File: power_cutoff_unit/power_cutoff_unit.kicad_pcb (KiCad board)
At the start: 2 copper layers, 0 parts

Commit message: 何したか覚えてないけど。
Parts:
- added BZ1: Buzzer, Buzzer_Beeper:Buzzer_12x9.5RM7.6, F.Cu at (213.0, 103.5)
- added C1: 0.022uF, Capacitor_SMD:C_0402_1005Metric, F.Cu at (103.9, 137.6)
- added C10: 1000u, Capacitor_THT:CP_Radial_D16.0mm_P7.50mm, F.Cu at (269.7, 84.0)
- added C11: 0.1u, Capacitor_SMD:C_0402_1005Metric, F.Cu at (103.9, 143.5)
- added C12: 10uF, Capacitor_SMD:C_0805_2012Metric, F.Cu at (177.0, 86.1)
- added C16: 0.1u, Capacitor_SMD:C_0402_1005Metric, F.Cu at (106.7, 137.6)
- added C18: 4.7uF, Capacitor_SMD:C_0603_1608Metric, F.Cu at (116.3, 123.3)
- added C2: 4700pF, Capacitor_SMD:C_0402_1005Metric, F.Cu at (103.9, 139.6)
- added C20: 0.1u, Capacitor_SMD:C_0402_1005Metric, F.Cu at (106.7, 139.6)
- added C21: 0.1u, Capacitor_SMD:C_0402_1005Metric, F.Cu at (106.7, 141.5)
- added C22: 4.7u, Capacitor_SMD:C_0805_2012Metric, F.Cu at (177.0, 89.1)
- added C23: 1u, Capacitor_SMD:C_0402_1005Metric, F.Cu at (106.7, 143.5)
- added C24: 0.1u, Capacitor_SMD:C_0402_1005Metric, F.Cu at (109.6, 137.6)
- added C25: 4.7u, Capacitor_SMD:C_0805_2012Metric, F.Cu at (177.0, 92.1)
- added C26: 4.7u, Capacitor_SMD:C_0805_2012Metric, F.Cu at (177.0, 95.2)
- added C27: 0.1u, Capacitor_SMD:C_0402_1005Metric, F.Cu at (109.6, 139.6)
- added C28: 0.1u, Capacitor_SMD:C_0402_1005Metric, F.Cu at (109.6, 141.5)
- added C29: 0.1u, Capacitor_SMD:C_0402_1005Metric, F.Cu at (109.6, 143.5)
- added C3: 1uF, Capacitor_SMD:C_0402_1005Metric, F.Cu at (103.9, 141.5)
- added C30: 0.1u, Capacitor_SMD:C_0402_1005Metric, F.Cu at (112.5, 137.6)
- added C31: 0.1u, Capacitor_SMD:C_0402_1005Metric, F.Cu at (112.5, 139.6)
- added C32: 0.1u, Capacitor_SMD:C_0402_1005Metric, F.Cu at (112.5, 141.5)
- added C33: 4.7u, Capacitor_SMD:C_0603_1608Metric, F.Cu at (116.3, 125.9)
- added C34: 1u, Capacitor_SMD:C_0402_1005Metric, F.Cu at (112.5, 143.5)
- added C4: 47uF, Capacitor_SMD:C_1210_3225Metric, F.Cu at (224.5, 114.8)
- added C5: 47uF, Capacitor_SMD:C_1210_3225Metric, F.Cu at (224.5, 119.0)
- added C6: 10uF, Capacitor_SMD:C_0805_2012Metric, F.Cu at (177.0, 80.1)
- added C7: 470u, Capacitor_THT:CP_Radial_D12.5mm_P5.00mm, F.Cu at (244.2, 79.0)
- added C8: 10uF, Capacitor_SMD:C_0805_2012Metric, F.Cu at (177.0, 83.1)
- added D10: LED, LED_SMD:LED_0603_1608Metric, F.Cu at (139.2, 87.5)
- added D14: LED, LED_SMD:LED_0603_1608Metric, F.Cu at (139.2, 90.1)
- added D15: Blue, LED_SMD:LED_0603_1608Metric_Pad1.05x0.95mm_HandSolder, F.Cu at (197.1, 108.0)
- added D16: LED, LED_SMD:LED_0603_1608Metric, F.Cu at (139.2, 92.7)
- added D17: SS2040FL, Diode_SMD:D_SOD-123F, F.Cu at (172.6, 106.4)
- added D18: LED, LED_SMD:LED_0603_1608Metric, F.Cu at (139.2, 95.3)
- added D19: LED, LED_SMD:LED_0603_1608Metric, F.Cu at (192.8, 82.5)
- added D2: LED, LED_SMD:LED_0603_1608Metric, F.Cu at (135.2, 87.5)
- added D20: LED, LED_SMD:LED_0603_1608Metric, F.Cu at (192.8, 60.8)
- added D21: LED, LED_SMD:LED_0603_1608Metric, F.Cu at (192.8, 65.0)
- added D22: LED, LED_SMD:LED_0603_1608Metric, F.Cu at (192.8, 69.0)
- added D23: LED, LED_SMD:LED_0603_1608Metric, F.Cu at (192.8, 73.0)
- added D24: LED, LED_SMD:LED_0603_1608Metric, F.Cu at (192.8, 77.5)
- added D3: LED, LED_SMD:LED_0603_1608Metric, F.Cu at (135.2, 90.1)
- added D4: LED, LED_SMD:LED_0603_1608Metric, F.Cu at (135.2, 92.7)
- added D5: SS2040FL, Diode_SMD:D_SOD-123F, F.Cu at (172.6, 99.7)
- added D6: LED, LED_SMD:LED_0603_1608Metric, F.Cu at (135.2, 95.3)
- added D7: LED, LED_SMD:LED_0603_1608Metric, F.Cu at (135.2, 97.9)
- added D8: SS2040FL, Diode_SMD:D_SOD-123F, F.Cu at (172.6, 103.1)
- added D9: LED, LED_SMD:LED_0603_1608Metric, F.Cu at (139.2, 84.9)
- added J1: Conn_01x02, Connector_AMASS:AMASS_XT60IPW-M_1x03_P7.20mm_Horizontal, F.Cu at (284.1, 126.8)
- added J10: Conn_01x02, Connector_AMASS:AMASS_XT30PW-M_1x02_P2.50mm_Horizontal, F.Cu at (219.0, 129.5)
- added J11: Conn_01x02_Pin, Connector_PinHeader_2.54mm:PinHeader_1x02_P2.54mm_Vertical, F.Cu at (203.5, 76.5)
- added J12: Conn_01x04, Connector_JST:JST_XH_B4B-XH-A_1x04_P2.50mm_Vertical, F.Cu at (197.5, 68.5)
- added J13: Conn_01x04, Connector_JST:JST_XH_B4B-XH-A_1x04_P2.50mm_Vertical, F.Cu at (197.5, 82.0)
- added J14: Conn_01x04, Connector_JST:JST_XH_B4B-XH-A_1x04_P2.50mm_Vertical, F.Cu at (224.5, 72.5)
- added J15: Conn_01x02, Connector_JST:JST_XH_B2B-XH-A_1x02_P2.50mm_Vertical, F.Cu at (204.5, 52.0)
- added J16: Conn_01x02, Connector_JST:JST_XH_B2B-XH-A_1x02_P2.50mm_Vertical, F.Cu at (213.2, 52.0)
- added J18: Conn_01x02, Connector_JST:JST_XH_B2B-XH-A_1x02_P2.50mm_Vertical, F.Cu at (222.0, 52.0)
- added J19: Conn_01x03, Connector_JST:JST_XH_B3B-XH-A_1x03_P2.50mm_Vertical, F.Cu at (207.0, 140.0)
- added J2: Conn_01x02, Connector_AMASS:AMASS_XT60IPW-M_1x03_P7.20mm_Horizontal, F.Cu at (246.6, 126.8)
- added J20: Conn_01x03, Connector_JST:JST_XH_B3B-XH-A_1x03_P2.50mm_Vertical, F.Cu at (197.5, 93.0)
- added J4: Conn_01x02, Connector_AMASS:AMASS_XT60PW-F_1x02_P7.20mm_Horizontal, F.Cu at (276.8, 65.7)
- added J6: Conn_01x02, Connector_AMASS:AMASS_XT60PW-F_1x02_P7.20mm_Horizontal, F.Cu at (251.1, 65.2)
- added JP1: SolderJumper_2_Open, Jumper:SolderJumper-2_P1.3mm_Open_RoundedPad1.0x1.5mm, B.Cu at (215.3, 72.5)
- added JP2: SolderJumper_2_Open, Jumper:SolderJumper-2_P1.3mm_Open_RoundedPad1.0x1.5mm, B.Cu at (215.3, 76.0)
- added JP3: SolderJumper_2_Open, Jumper:SolderJumper-2_P1.3mm_Open_RoundedPad1.0x1.5mm, B.Cu at (215.3, 79.6)
- added K1: T9GS1L14-5, GN10RELAY:T9G, F.Cu at (283.2, 113.2)
- added K2: G5Q-1-DC5, GN10RELAY:G5Q-1, F.Cu at (254.9, 109.8)
- added L1: 4.7u, GN10:DEM2818C, F.Cu at (217.0, 116.0)
- added Q1: SSM3K341R, Package_TO_SOT_SMD:SOT-23_Handsoldering, B.Cu at (227.5, 97.3)
- added Q2: SSM3K341R, Package_TO_SOT_SMD:SOT-23_Handsoldering, B.Cu at (227.5, 102.0)
- added Q3: SSM3K341R, Package_TO_SOT_SMD:SOT-23_Handsoldering, B.Cu at (227.5, 106.8)
- added Q5: BSS138, Package_TO_SOT_SMD:SOT-23, F.Cu at (207.6, 91.5)
- added R1: 100K, Resistor_SMD:R_0603_1608Metric, F.Cu at (116.3, 128.4)
- added R10: 1K, Resistor_SMD:R_0603_1608Metric, F.Cu at (120.3, 123.3)
- added R11: 20K, Resistor_SMD:R_0603_1608Metric, F.Cu at (120.3, 125.9)
- added R12: 4.7K, Resistor_SMD:R_0603_1608Metric, F.Cu at (120.3, 128.4)
- added R13: 470, Resistor_SMD:R_0603_1608Metric, F.Cu at (120.3, 130.9)
- added R14: 20K, Resistor_SMD:R_0603_1608Metric, F.Cu at (120.3, 133.4)
- added R15: 25, Package_TO_SOT_THT:TO-220-2_Vertical, F.Cu at (258.2, 91.0)
- added R16: 1K, Resistor_SMD:R_0402_1005Metric, F.Cu at (171.5, 64.0)
- added R17: 1K, Resistor_SMD:R_0603_1608Metric, F.Cu at (120.3, 135.9)
- added R18: 20K, Resistor_SMD:R_0603_1608Metric, F.Cu at (120.3, 138.4)
- added R19: 1K, Resistor_SMD:R_0402_1005Metric, F.Cu at (171.5, 66.0)
- added R2: 34K, Resistor_SMD:R_0402_1005Metric, F.Cu at (171.5, 58.0)
- added R20: 25, Package_TO_SOT_THT:TO-220-2_Vertical, F.Cu at (242.0, 96.4)
- added R21: 4.7K, Resistor_SMD:R_0603_1608Metric, F.Cu at (120.3, 140.9)
- added R27: 20K, Resistor_SMD:R_0603_1608Metric, F.Cu at (124.3, 123.3)
- added R28: 20K, Resistor_SMD:R_0603_1608Metric, F.Cu at (124.3, 125.9)
- added R29: 20K, Resistor_SMD:R_0603_1608Metric, F.Cu at (124.3, 128.4)
- added R3: 24K, Resistor_SMD:R_0603_1608Metric, F.Cu at (116.3, 130.9)
- added R30: 20K, Resistor_SMD:R_0603_1608Metric, F.Cu at (124.3, 130.9)
- added R31: 1K, Resistor_SMD:R_0603_1608Metric, F.Cu at (124.3, 133.4)
- added R32: 1K, Resistor_SMD:R_0603_1608Metric, F.Cu at (124.3, 135.9)
- added R33: 1K, Resistor_SMD:R_0603_1608Metric, F.Cu at (124.3, 138.4)
- added R34: 120, Resistor_SMD:R_0603_1608Metric, F.Cu at (124.3, 140.9)
- added R35: 1K, Resistor_SMD:R_0603_1608Metric, F.Cu at (128.3, 123.3)
- added R36: 10K, Resistor_SMD:R_0603_1608Metric, F.Cu at (128.3, 125.9)
- added R37: 470, Resistor_SMD:R_0603_1608Metric, F.Cu at (128.3, 128.4)
- added R38: 20K, Resistor_SMD:R_0603_1608Metric, F.Cu at (128.3, 130.9)
- added R39: 1K, Resistor_SMD:R_0603_1608Metric, F.Cu at (128.3, 133.4)
- added R4: 4.7K, Resistor_SMD:R_0603_1608Metric, F.Cu at (116.3, 133.4)
- added R40: 1K, Resistor_SMD:R_0603_1608Metric, F.Cu at (128.3, 135.9)
- added R41: 1K, Resistor_SMD:R_0603_1608Metric, F.Cu at (128.3, 138.4)
- added R42: 1K, Resistor_SMD:R_0603_1608Metric, F.Cu at (128.3, 140.9)
- added R43: 1K, Resistor_SMD:R_0603_1608Metric, F.Cu at (132.3, 123.3)
- added R44: 1K, Resistor_SMD:R_0603_1608Metric, F.Cu at (132.3, 125.9)
- added R45: 10K, Resistor_SMD:R_0603_1608Metric, F.Cu at (132.3, 128.4)
- added R46: 10K, Resistor_SMD:R_0603_1608Metric, F.Cu at (132.3, 130.9)
- added R47: 10K, Resistor_SMD:R_0603_1608Metric, F.Cu at (132.3, 133.4)
- added R48: 10K, Resistor_SMD:R_0603_1608Metric, F.Cu at (132.3, 135.9)
- added R49: 10K, Resistor_SMD:R_0603_1608Metric, F.Cu at (132.3, 138.4)
- added R5: 6.49K, Resistor_SMD:R_0402_1005Metric, F.Cu at (171.5, 60.0)
- added R7: 4.7K, Resistor_SMD:R_0603_1608Metric, F.Cu at (116.3, 138.4)
- added R8: 4.7K, Resistor_SMD:R_0603_1608Metric, F.Cu at (116.3, 140.9)
- added R9: 1K, Resistor_SMD:R_0402_1005Metric, F.Cu at (171.5, 62.0)
- added SW1: SW_Push, GN10:SKRPABE010, F.Cu at (200.1, 54.0)
- added SW2: SW_DIP_x02, Button_Switch_SMD:SW_DIP_SPSTx02_Slide_Omron_A6H-2101_W6.15mm_P1.27mm, F.Cu at (216.4, 62.1)
- added SW3: SW_DIP_x02, Button_Switch_SMD:SW_DIP_SPSTx02_Slide_Omron_A6H-2101_W6.15mm_P1.27mm, F.Cu at (195.0, 139.0)
- added U1: LMZ14201H, GN10:LMZ14201H, F.Cu at (258.0, 136.5)
- added U3: MIC4427, Package_SO:SOIC-8_3.9x4.9mm_P1.27mm, B.Cu at (228.0, 90.9)
- added U4: ADuM120N, Package_SO:SOIC-8_3.9x4.9mm_P1.27mm, F.Cu at (223.0, 83.1)
- added U5: LMR50410Y3FQDBVRQ1, Package_TO_SOT_SMD:SOT-23-6, F.Cu at (217.5, 121.1)
- added U6: MCP2562-E-SN, Package_SO:SOIC-8_3.9x4.9mm_P1.27mm, F.Cu at (207.0, 63.5)
- added U7: STM32F303K8Tx, Package_QFP:LQFP-32_7x7mm_P0.8mm, F.Cu at (215.0, 73.0)
- added U8: MOUDLE-SEEEDUINO-XIAO-ESP32C3, RF_Module:MCU_Seeed_ESP32C3, F.Cu at (202.9, 121.0)

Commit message: PCBに入ったけどコンデンサの放電用抵抗を小さくしたい。
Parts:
- removed U8: MOUDLE-SEEEDUINO-XIAO-ESP32C3, RF_Module:MCU_Seeed_ESP32C3
- added U2: MOUDLE-SEEEDUINO-XIAO-ESP32C3, RF_Module:MCU_Seeed_ESP32C3, F.Cu at (-132.0, 145.6)
- C1: value 0.022uF -> 0.022u
- C12: value 10uF -> 10u
- C18: value 4.7uF -> 4.7u
- C2: value 4700pF -> 4700p
- J1, J2: footprint Connector_AMASS:AMASS_XT60IPW-M_1x03_P7.20mm_Horizontal -> Connector_AMASS:AMASS_XT60PW-M_1x02_P7.20mm_Horizontal
- JP1, JP2, JP3, Q1, Q2, Q3, U3: moved to F.Cu
- R15, R20: value 25 -> 30; footprint Package_TO_SOT_THT:TO-220-2_Vertical -> Package_TO_SOT_SMD:TO-263-2_TabPin1
- moved J1 547.4 mm to (-256.8, 42.3), turned to 0 degrees
- moved J2 493.1 mm to (-239.2, 42.3), turned to 0 degrees
- moved U1 486.2 mm to (-226.0, 90.3), turned to 0 degrees
- moved C4 483.7 mm to (-258.2, 84.7)
- moved C5 483.7 mm to (-258.2, 89.0)
- moved L1 472.2 mm to (-252.6, 165.9)
- moved U6 470.6 mm to (-245.4, 193.0)
- moved U5 457.3 mm to (-237.8, 163.8), turned to 0 degrees
- moved K1 456.8 mm to (-169.2, 49.8), turned to 0 degrees
- moved J11 452.6 mm to (-234.2, 191.7)
- moved J10 445.3 mm to (-225.9, 147.2), turned to 0 degrees
- moved J12 430.6 mm to (-216.4, 187.4), turned to 0 degrees
- moved R2 429.5 mm to (-256.6, 92.7)
- moved R5 429.5 mm to (-256.6, 94.7)
- moved J13 429.1 mm to (-216.4, 195.2), turned to 0 degrees
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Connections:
- net VDD renamed +5VA

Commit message: 配置考え始めた
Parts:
- removed C11: 0.1u, Capacitor_SMD:C_0402_1005Metric
- removed C3: 1uF, Capacitor_SMD:C_0402_1005Metric
- removed J18: Conn_01x02, Connector_JST:JST_XH_B2B-XH-A_1x02_P2.50mm_Vertical
- removed J19: Conn_01x03, Connector_JST:JST_XH_B3B-XH-A_1x03_P2.50mm_Vertical
- removed R49: 10K, Resistor_SMD:R_0603_1608Metric
- D8, Q2, R13, R14, R20, R34, R47, R48, U6: moved to B.Cu
- J10: footprint Connector_AMASS:AMASS_XT30PW-M_1x02_P2.50mm_Horizontal -> Connector_AMASS:AMASS_XT30U-M_1x02_P5.0mm_Vertical
- R15: value 30 -> 50; moved to B.Cu
- R3, R32, R4: footprint Resistor_SMD:R_0603_1608Metric -> Resistor_SMD:R_0402_1005Metric
- moved R7 439.6 mm to (193.5, 62.5), turned to 180 degrees
- moved J2 427.4 mm to (187.9, 57.6)
- moved J1 423.5 mm to (166.4, 57.6)
- moved D2 416.9 mm to (190.5, 62.5)
- moved R8 405.6 mm to (159.5, 55.2), turned to -90 degrees
- moved C5 399.3 mm to (140.6, 70.0)
- moved C4 399.3 mm to (140.6, 66.5)
- moved R2 393.1 mm to (135.5, 65.5), turned to 180 degrees
- moved R5 391.2 mm to (133.5, 65.5)
- moved R1 390.2 mm to (135.5, 56.0), turned to -90 degrees
- moved R3 388.4 mm to (133.5, 56.0), turned to 180 degrees
- moved R4 386.7 mm to (131.5, 56.0), turned to 180 degrees
- moved D3 385.4 mm to (159.5, 58.3), turned to 90 degrees
- moved C6 383.5 mm to (140.6, 52.5)
- moved C1 379.3 mm to (135.5, 67.5), turned to 180 degrees
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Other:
- board outline added: 100 x 75 mm

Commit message: PCBの配置考え中
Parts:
- J14: footprint Connector_JST:JST_XH_B4B-XH-A_1x04_P2.50mm_Vertical -> Connector_PinHeader_2.54mm:PinHeader_1x04_P2.54mm_Vertical
- J20: footprint Connector_JST:JST_XH_B3B-XH-A_1x03_P2.50mm_Vertical -> Connector_PinHeader_2.54mm:PinHeader_1x03_P2.54mm_Vertical
- R15, R20: moved to F.Cu
- moved R11 91.5 mm to (67.2, 126.5)
- moved R27 91.5 mm to (59.7, 139.0)
- moved R28 91.5 mm to (59.7, 137.0)
- moved C12 91.5 mm to (104.0, 121.5)
- moved C16 91.5 mm to (71.0, 136.0)
- moved C18 91.5 mm to (71.0, 134.5)
- moved C20 91.5 mm to (60.0, 142.0)
- moved C21 91.5 mm to (65.0, 142.0)
- moved C22 91.5 mm to (7.00, 91.4)
- moved C23 91.5 mm to (-8.53, 98.4)
- moved C24 91.5 mm to (-5.66, 92.5)
- moved C25 91.5 mm to (7.00, 94.4)
- moved C26 91.5 mm to (7.00, 97.4)
- moved C27 91.5 mm to (-113.5, 181.7)
- moved C28 91.5 mm to (-113.5, 183.6)
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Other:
- board size 100 x 75 mm -> 237 x 99 mm

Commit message: 大電流部品の主な配置を考えた。
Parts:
- added REF**: MountingHole_3.2mm_M3, MountingHole:MountingHole_3.2mm_M3, F.Cu at (123.5, 67.5)
- added REF**: MountingHole_3.2mm_M3, MountingHole:MountingHole_3.2mm_M3, F.Cu at (215.5, 134.5)
- added REF**: MountingHole_3.2mm_M3, MountingHole:MountingHole_3.2mm_M3, F.Cu at (123.5, 134.5)
- added REF**: MountingHole_3.2mm_M3, MountingHole:MountingHole_3.2mm_M3, F.Cu at (215.5, 67.5)
- R15: moved to B.Cu
- moved J10 110.8 mm to (130.2, 67.3), turned to 0 degrees
- moved K2 58.9 mm to (197.5, 81.9), turned to 0 degrees
- moved U2 51.7 mm to (137.8, 178.7)
- moved R15 47.3 mm to (187.4, 94.6), turned to 0 degrees
- moved J16 44.0 mm to (118.9, 165.7)
- moved R20 43.1 mm to (201.3, 102.3), turned to -90 degrees
- moved J15 35.2 mm to (133.5, 158.7)
- moved J2 33.8 mm to (200.1, 75.7)
- moved J6 32.9 mm to (199.0, 129.9)
- moved C7 32.6 mm to (205.5, 120.0)
- moved K1 30.3 mm to (168.7, 88.4)
- moved BZ1 30.0 mm to (145.2, 119.0)
- moved J12 30.0 mm to (123.0, 121.0)
- moved J13 30.0 mm to (123.0, 107.0)
- moved J14 30.0 mm to (149.0, 100.9)
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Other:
- board size 237 x 99 mm -> 207 x 86 mm

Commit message: 重要な制御系部品の配置を少し考えた。
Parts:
- C16, C18, U3: moved to B.Cu
- moved L1 162.4 mm to (130.3, 80.5)
- moved U5 149.7 mm to (132.1, 76.7), turned to 180 degrees
- moved C23 139.5 mm to (129.3, 76.7), turned to -90 degrees
- moved C24 139.4 mm to (133.1, 79.0), turned to 180 degrees
- moved D17 132.5 mm to (132.1, 73.7)
- moved SW3 131.5 mm to (152.4, 120.7), turned to -90 degrees
- moved C26 131.3 mm to (137.1, 80.3), turned to 90 degrees
- moved C25 128.9 mm to (135.1, 80.3), turned to 90 degrees
- moved C22 121.6 mm to (127.7, 76.7), turned to -90 degrees
- moved U3 112.8 mm to (173.4, 96.6)
- moved C16 110.0 mm to (171.9, 92.1), turned to 180 degrees
- moved C18 110.0 mm to (171.9, 90.6), turned to 180 degrees
- moved C20 109.6 mm to (159.6, 96.2)
- moved C21 109.0 mm to (163.4, 95.0)
- moved R27 108.7 mm to (158.3, 93.2)
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
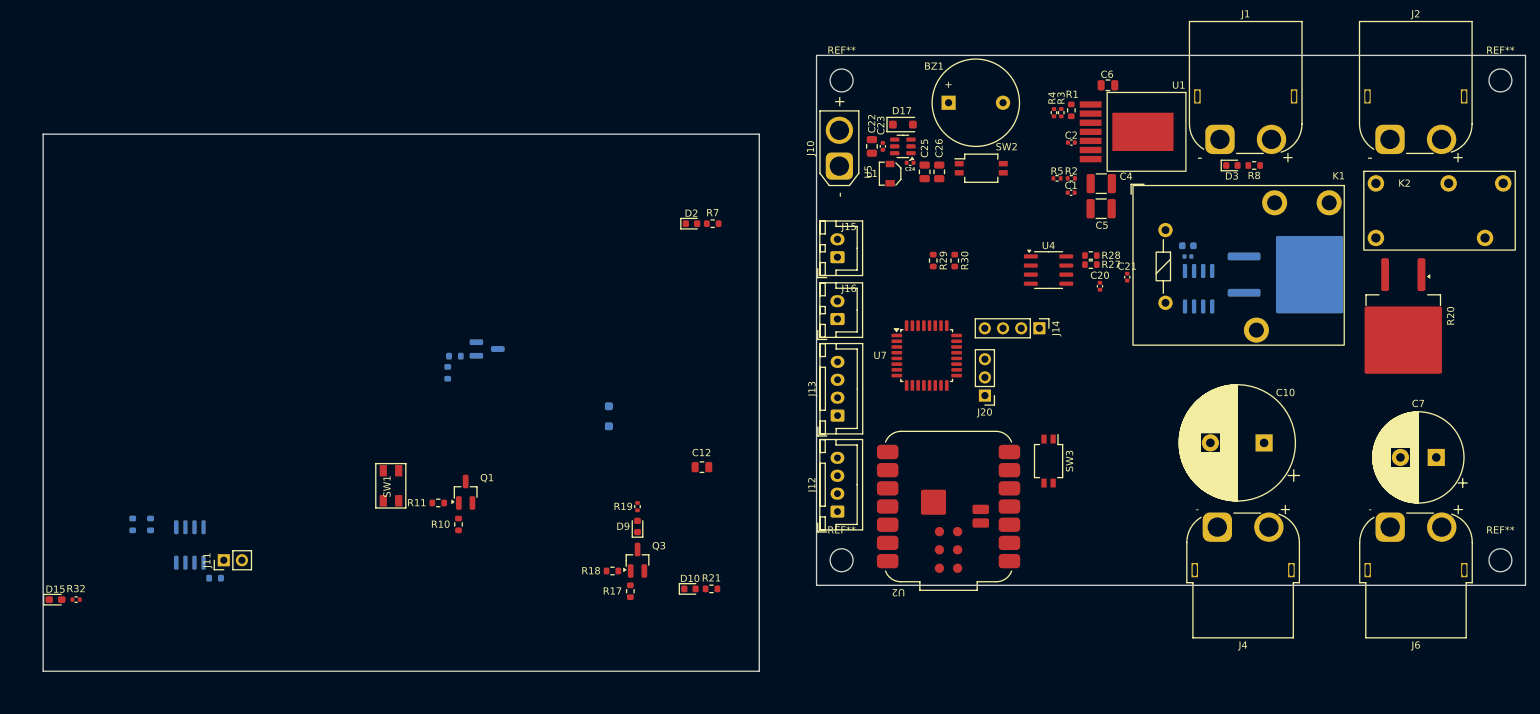
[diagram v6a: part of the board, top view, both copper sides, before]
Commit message: 高額だし、大きいので5Vラインのスイッチングレギュレーターを変更。
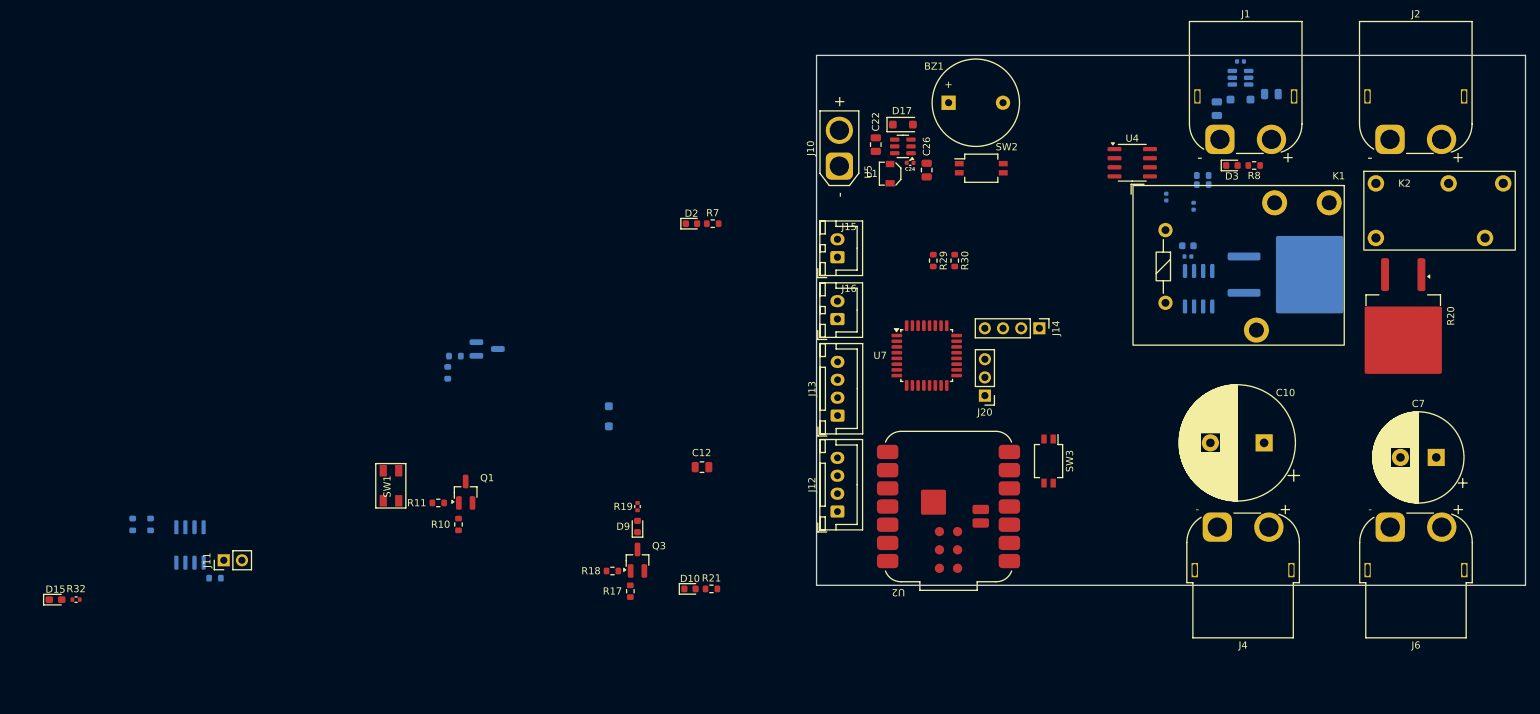
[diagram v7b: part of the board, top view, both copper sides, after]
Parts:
- removed C1: 0.022u, Capacitor_SMD:C_0402_1005Metric
- removed C2: 4700p, Capacitor_SMD:C_0402_1005Metric
- removed C23: 1u, Capacitor_SMD:C_0402_1005Metric
- removed C25: 4.7u, Capacitor_SMD:C_0805_2012Metric
- removed C4, C5: 47uF, Capacitor_SMD:C_1210_3225Metric
- removed C6: 10uF, Capacitor_SMD:C_0805_2012Metric
- removed R1: 100K, Resistor_SMD:R_0603_1608Metric
- removed R2: 34K, Resistor_SMD:R_0402_1005Metric
- removed R3: 24K, Resistor_SMD:R_0402_1005Metric
- removed R4: 4.7K, Resistor_SMD:R_0402_1005Metric
- removed R5: 6.49K, Resistor_SMD:R_0402_1005Metric
- removed REF** (x4): MountingHole_3.2mm_M3, MountingHole:MountingHole_3.2mm_M3
- removed U1: LMZ14201H, GN10:LMZ14201H
- added C11: 10u, Capacitor_SMD:C_0805_2012Metric, B.Cu at (183.5, 69.4)
- added C3: 2.2u, Capacitor_SMD:C_0805_2012Metric, B.Cu at (175.9, 71.4)
- added C9: 0.1u, Capacitor_SMD:C_0402_1005Metric, B.Cu at (179.2, 64.8)
- added D1: SS2040FL, Diode_SMD:D_SOD-123F, B.Cu at (179.2, 70.2)
- added U8: LMR50410Y5FQDBVRQ1, Package_TO_SOT_SMD:SOT-23-6, B.Cu at (179.2, 67.1)
- C20, C21, R27, R28: moved to B.Cu
- C22: value 4.7u -> 2.2u
- C26: value 4.7u -> 10u
- L1: value 4.7u -> 3.3u
- moved R27 19.2 mm to (173.9, 82.0), turned to 180 degrees
- moved R28 19.2 mm to (173.9, 80.8), turned to 180 degrees
- moved U4 19.0 mm to (164.1, 79.0)
- moved C20 17.2 mm to (172.7, 85.1)
- moved C21 12.4 mm to (168.8, 83.8)
- moved C26 1.77 mm to (135.4, 80.0)
- moved C22 0.59 mm to (128.3, 76.5)
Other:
- board size 207 x 86 mm -> 99 x 74 mm
